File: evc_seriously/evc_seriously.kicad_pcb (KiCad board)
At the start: 2 copper layers, 58 parts, among them J1 Screw_Terminal_01x10, J2 Conn_ARM_JTAG_SWD_10, J3 J_IN, J4 J_OUT, SW1 SW_Push, U1 TCA9517, U2 MPM3510A, U3 MPM3510A, U4 STM32F303K8Tx, U5 MIC2981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

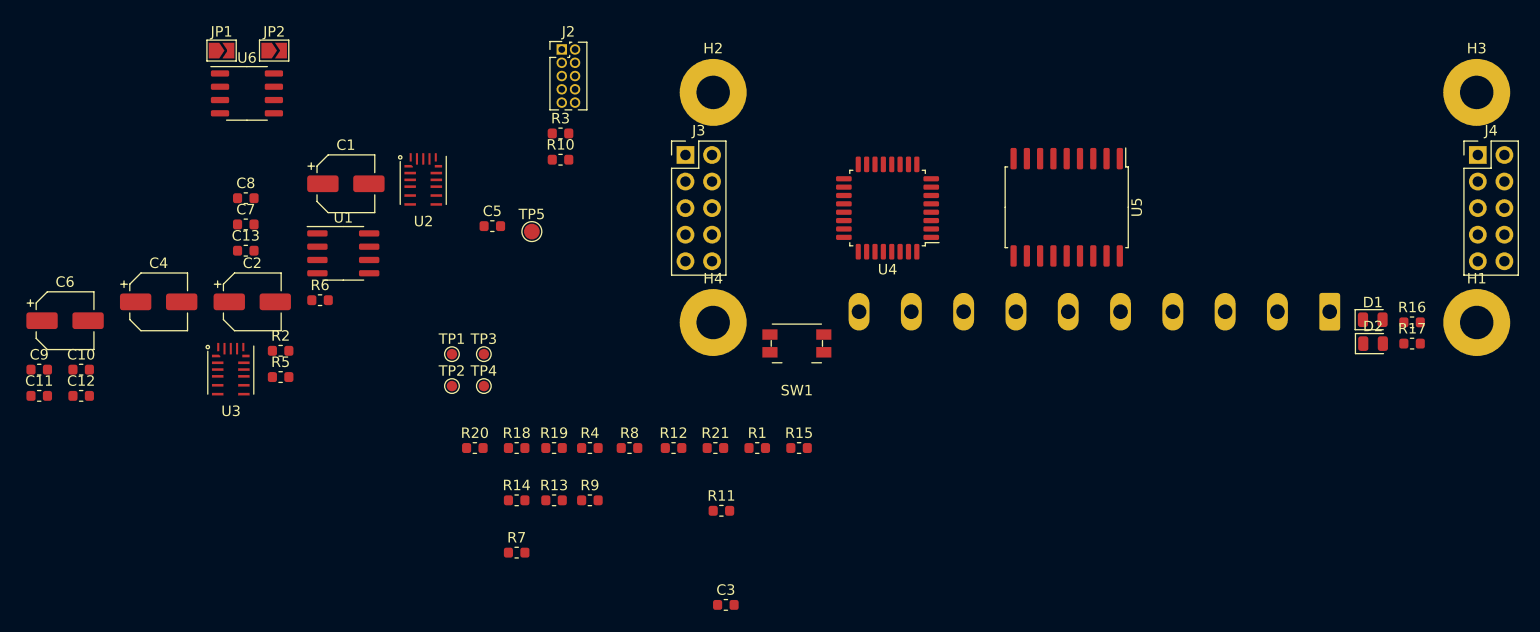
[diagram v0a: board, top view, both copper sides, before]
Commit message: More routing
- Finish routing power nets
- Start routing data/enable lines
- Swap a bunch of microcontroller pins to reduce hopping
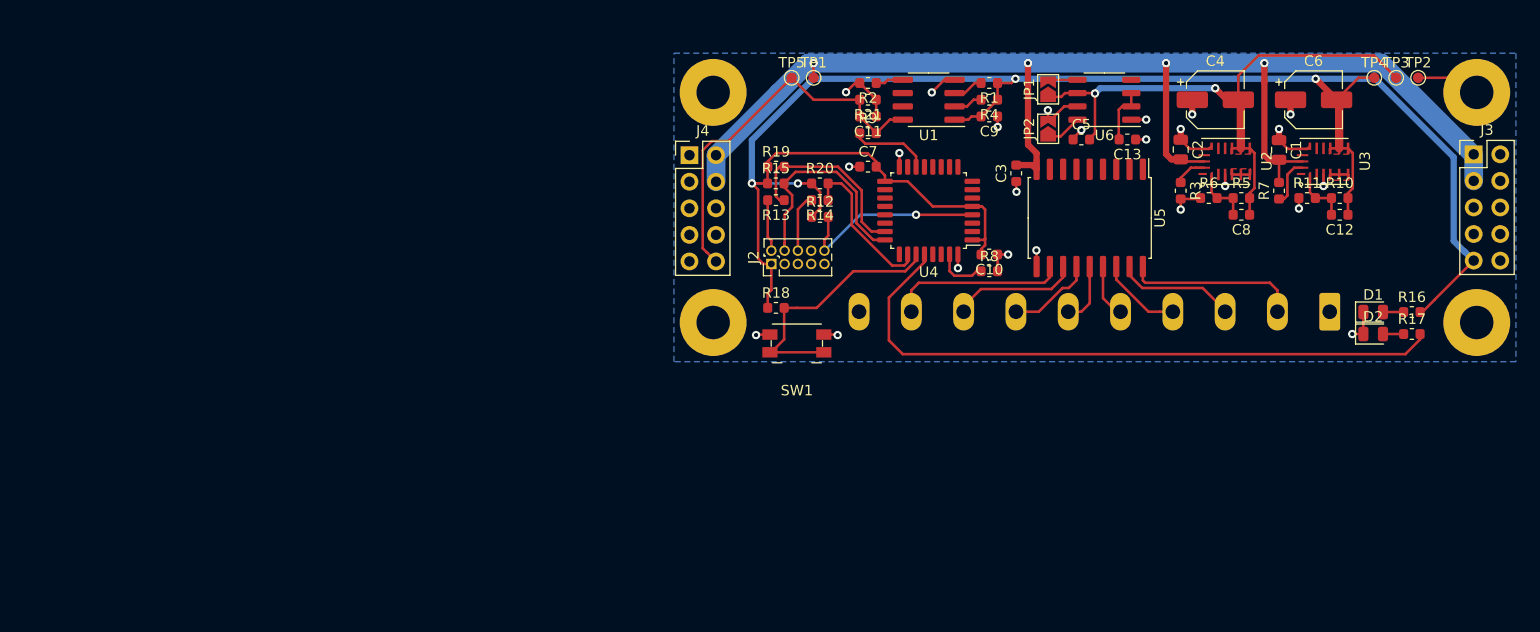
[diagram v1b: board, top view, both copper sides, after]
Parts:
- C1, C2: footprint Capacitor_SMD:CP_Elec_5x5.8 -> Capacitor_SMD:C_0805_2012Metric
- TP5: footprint TestPoint:TestPoint_Pad_D1.5mm -> TestPoint:TestPoint_Pad_D1.0mm
- moved C12 121.6 mm to (203.9, 115.7), turned to 180 degrees
- moved C6 121.2 mm to (201.4, 104.7)
- moved U3 106.6 mm to (202.6, 110.6), turned to 90 degrees
- moved C4 102.9 mm to (192.0, 104.7)
- moved TP2 97.0 mm to (211.4, 102.6)
- moved C8 95.2 mm to (194.5, 115.7), turned to 180 degrees
- moved C9 94.0 mm to (170.4, 106.3), turned to 180 degrees
- moved R5 93.4 mm to (194.5, 114.1)
- moved TP3 91.1 mm to (209.3, 102.6)
- moved TP4 90.1 mm to (207.2, 102.6)
- moved C2 90.0 mm to (188.7, 109.5), turned to 270 degrees
- moved C1 89.3 mm to (198.1, 109.5), turned to 270 degrees
- moved C10 87.5 mm to (170.4, 119.5), turned to 180 degrees
- moved R6 85.5 mm to (191.4, 114.1)
- moved C13 85.0 mm to (183.6, 108.5), turned to 180 degrees
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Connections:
- H1 pad 1: Net-(H1-Pad1) -> GND
- H2 pad 1: Net-(H2-Pad1) -> GND
- H3 pad 1: Net-(H3-Pad1) -> GND
- H4 pad 1: Net-(H4-Pad1) -> GND
- J3 pad 1: GND -> +24V
- J3 pad 10: +24V -> GND
- J3 pad 3: GND -> +24V
- J3 pad 5: GND -> /SDA_A
- J3 pad 6: +3V3 -> GND
- J3 pad 8: /SDA_A -> GND
- J3 pad 9: +24V -> +3V3
- J4 pad 10: +24V -> +3V3_B
- J4 pad 2: GND -> +24V
- J4 pad 4: GND -> +24V
- J4 pad 6: +3V3_B -> /SDA_B
- J4 pad 7: /SCL_B -> GND
- J4 pad 8: /SDA_B -> /SCL_B
- J4 pad 9: +24V -> GND
- JP1 pad 2: /VFIL+ -> /VFIL-
- JP2 pad 1: /VFIL- -> /VFIL+
- R9 pad 1: Net-(R9-Pad1) -> /SENSE
- U4 pad 14: Net-(U4-Pad14) -> /SENSE
- U4 pad 20: /USR_SW -> Net-(U4-Pad20)
- U4 pad 21: /USR_LED -> /I2C_EN
- U4 pad 22: Net-(U4-Pad22) -> /5V_EN
- U4 pad 27: /5V_EN -> /USR_SW
- U4 pad 28: /I2C_EN -> /USR_LED
- U4 pad 3: Net-(R9-Pad1) -> Net-(U4-Pad3)
- U6 pad 5: /VFIL+ -> /VFIL-
- U6 pad 8: /VFIL- -> /VFIL+
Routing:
- net +3V3: track 0.00 -> 180.4 mm, vias 0 -> 4
- net +24V: track 0.00 -> 126.2 mm, vias 0 -> 4
- net /USR_LED: track 0.00 -> 62.1 mm
- net +5V: track 0.00 -> 56.6 mm, vias 0 -> 2
- net GND: track 0.00 -> 56.3 mm, vias 0 -> 24
- net +3V3_B: track 0.00 -> 37.6 mm
- net /USR_SW: track 0.00 -> 25.7 mm
- net /SWDCLK: track 0.00 -> 22.3 mm
- net /SWDIO: track 0.00 -> 19.1 mm
- net /NRST: track 0.00 -> 18.9 mm, vias 0 -> 1
- net /GRID: track 0.00 -> 16.8 mm
- net /SEG_A: track 0.00 -> 16.6 mm
- net /SWO: track 0.00 -> 15.1 mm
- net /SEG_G: track 0.00 -> 12.2 mm
- net /SEG_B: track 0.00 -> 11.5 mm
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- added copper zone on F.Cu, net +3V3
- added copper zone on F.Cu, net +5V
- added copper zone on B.Cu, net GND
- added copper zone on F.Cu, net Net-(U2-Pad4)
- added copper zone on F.Cu, net Net-(U3-Pad4)

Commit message: Final changes for rev 1.1
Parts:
- moved C3 3.95 mm to (172.0, 107.9), turned to 0 degrees
- moved J2 0.91 mm to (149.7, 119.5)
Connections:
- JP1 pad 2: /VFIL- -> /VFIL+
- JP2 pad 1: /VFIL+ -> /VFIL-
- U4 pad 22: /5V_EN -> Net-(U4-Pad22)
- U4 pad 3: Net-(U4-Pad3) -> /5V_EN
- U6 pad 5: /VFIL- -> /VFIL+
- U6 pad 8: /VFIL+ -> /VFIL-
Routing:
- net /SCL_A: track 2.80 -> 79.0 mm, vias 0 -> 3
- net /SDA_A: track 2.94 -> 79.1 mm, vias 0 -> 3
- net /VFIL-: track 2.88 -> 47.8 mm, vias 0 -> 1
- net /VFIL+: track 3.47 -> 47.7 mm, vias 0 -> 2
- net /FIL_PWM: track 0.00 -> 41.2 mm, vias 0 -> 2
- net /SCL_B: track 0.00 -> 32.6 mm, vias 0 -> 2
- net /SDA_B: track 0.00 -> 27.9 mm, vias 0 -> 2
- net /5V_EN: track 3.09 -> 27.2 mm, vias 0 -> 2
- net Net-(U4-Pad6): track 0.00 -> 20.3 mm
- net /I2C_EN: track 2.66 -> 22.7 mm, vias 0 -> 2
- net Net-(U4-Pad7): track 0.00 -> 18.9 mm
- net Net-(U4-Pad10): track 0.00 -> 17.6 mm
- net Net-(U4-Pad8): track 0.00 -> 17.5 mm
- net Net-(U4-Pad9): track 0.00 -> 17.2 mm
- net Net-(U4-Pad11): track 0.00 -> 17.1 mm
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- removed copper zone on F.Cu, net +3V3
- removed copper zone on F.Cu, net +5V
- removed copper zone on F.Cu, net Net-(U2-Pad4)
- removed copper zone on F.Cu, net Net-(U3-Pad4)
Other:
- board outline added: 81 x 30 mm
- board text added: "2020"
- board text added: "EVC"
- board text added: "H"
- board text added: "SRSLY"
- board text added: "v1.1"
